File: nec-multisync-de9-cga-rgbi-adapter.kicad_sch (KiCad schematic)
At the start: 2 parts, among them J1 DE9_Plug, J2 DE15_Receptacle_HighDensity

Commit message: V1 to Fab
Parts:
- added J3: DIN-8, CUI_SDS_80J:CUI_SDS-80J, symbol Connector:DIN-8
- added JP1, JP4, JP5, JP6, JP7: Jumper_2_Bridged, Jumper:SolderJumper-2_P1.3mm_Bridged_Pad1.0x1.5mm, symbol Jumper:Jumper_2_Bridged
- J1: footprint (none) -> Connector_Dsub:DSUB-9_Male_Horizontal_P2.77x2.84mm_EdgePinOffset7.70mm_Housed_MountingHolesOffset9.12mm
- J2: footprint (none) -> Connector_TE_AMP_HD15:FIXED-1-1734530-1
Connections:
- net EGA_Blue0: now also J3.8
- net EGA_Green0: now also JP6.1 (A)
- net EGA_Green1_Intensity: now also JP1.2 (B)
- net EGA_Red0: now also JP7.2 (B)
- net GND: now also J3.2
- net HSync: now also JP5.1 (A)
- net VSync: now also JP4.2 (B)
- new net: J3.5, JP5.2 (B)
- new net: J3.6, JP6.2 (B)
- new net: J3.7, JP7.1 (A)
- new net: J3.1, JP1.1 (A)
- new net: J3.4, JP4.1 (A)
- no-connect marks 6 -> 7
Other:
- note added: "From IBM PC"
- note added: "From Japanese PC"
- note added: "NOT ACCURATE PIN NUMBERS Flipped from reality because we expect a male-male cable"
- note removed: "TODO: Din8"
- note removed: "To IBM PC"

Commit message: Update to NOTWORKING
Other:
- note added: "TODO: This does not work on MultiSync 3D yet (no wakeup)"
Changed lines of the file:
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@@
+    (effects (font (size 1.27 1.27)) (justify left bottom))
+  )
+  (text "TODO: This does not work on MultiSync 3D yet (no wakeup)"
+    (at 92.71 131.445 0)
     (effects (font (size 1.27 1.27)) (justify left bottom))
   )

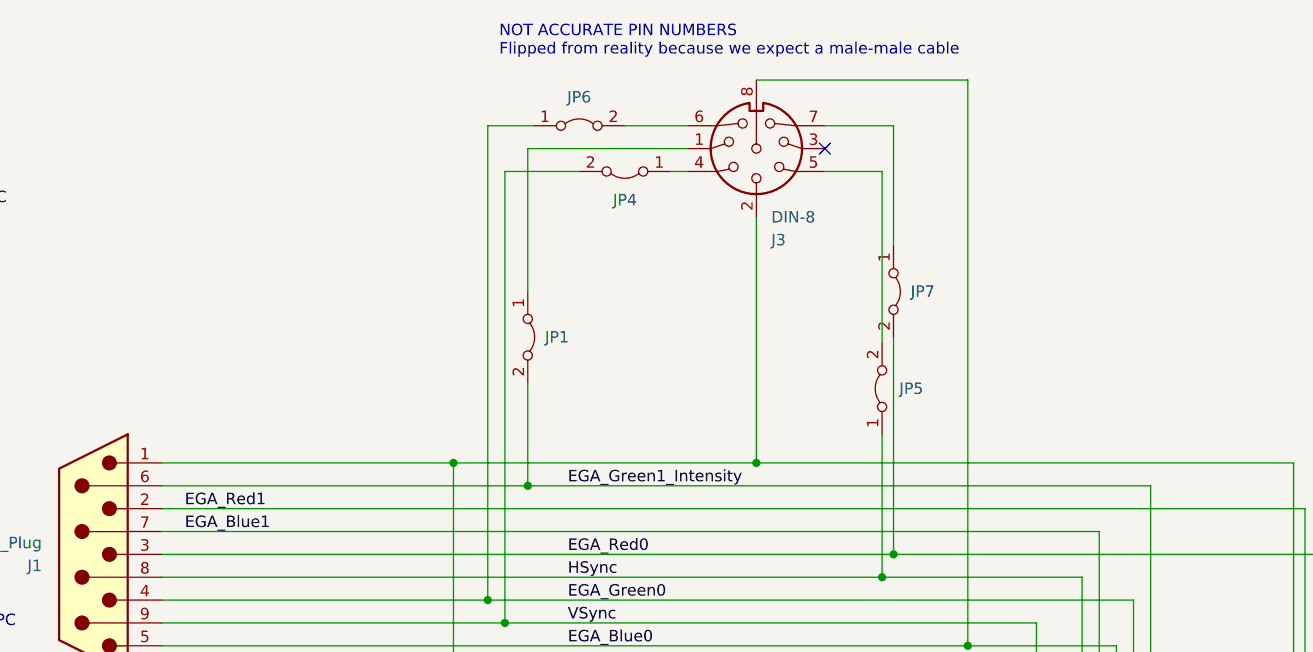
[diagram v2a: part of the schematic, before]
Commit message: Maybe reverse my bonehead fuckup of feeding 12V to the MultiSync's signal input
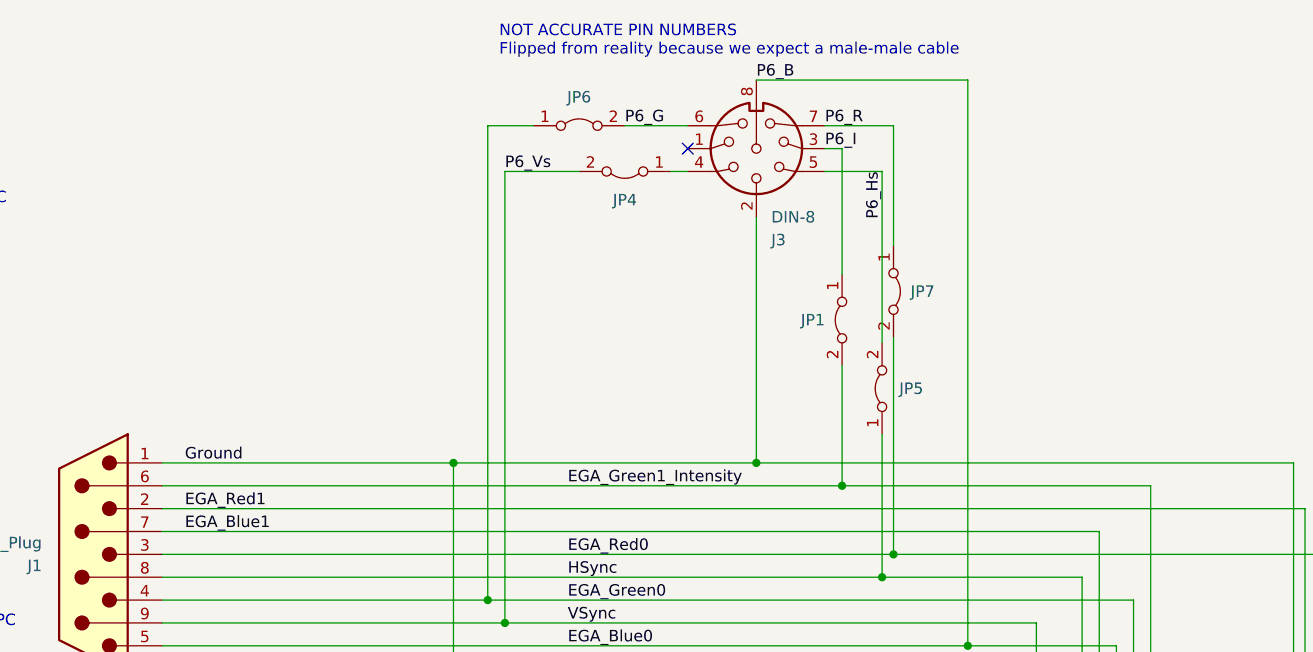
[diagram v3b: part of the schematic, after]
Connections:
- net P6_Hs: now reaches J3.5, JP5.2 (B)
- net P6_G: now reaches J3.6, JP6.2 (B)
- net P6_R: now reaches J3.7, JP7.1 (A)
- net at J3.1: no longer JP1.1 (A)
- net P6_I: now reaches J3.3
- net P6_I: now also JP1.1 (A)
- net VSync renamed P6_Vs
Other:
- moved on the sheet: JP1
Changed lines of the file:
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@@
   (junction (at 88.9 67.31) (diameter 0) (color 0 0 0 0)
   )
+  (junction (at 132.08 69.85) (diameter 0) (color 0 0 0 0)
+  )
   (junction (at 122.555 67.31) (diameter 0) (color 0 0 0 0)
-  )
-  (junction (at 97.155 69.85) (diameter 0) (color 0 0 0 0)
   )
   (junction (at 137.795 77.47) (diameter 0) (color 0 0 0 0)
@@
   (no_connect (at 195.58 102.235))
   (no_connect (at 195.58 97.155))
-  (no_connect (at 130.175 32.385))
   (no_connect (at 195.58 104.775))
   (no_connect (at 210.82 89.535))
   (no_connect (at 195.58 92.075))
+  (no_connect (at 114.935 32.385))
   (wire (pts (xy 137.795 29.845) (xy 137.795 43.18))
     (stroke (width 0) (type default))
   )
-  (wire (pts (xy 114.935 32.385) (xy 97.155 32.385))
+  (wire (pts (xy 132.08 69.85) (xy 166.37 69.85))
     (stroke (width 0) (type default))
   )
@@
     (stroke (width 0) (type default))
   )
-  (wire (pts (xy 97.155 32.385) (xy 97.155 48.26))
-    (stroke (width 0) (type default))
-  )
   (wire (pts (xy 226.695 104.775) (xy 210.82 104.775))
     (stroke (width 0) (type default))
   )
+  (wire (pts (xy 132.08 56.515) (xy 132.08 69.85))
+    (stroke (width 0) (type default))
+  )
   (wire (pts (xy 122.555 40.005) (xy 122.555 67.31))
     (stroke (width 0) (type default))
@@
     (stroke (width 0) (type default))
   )
-  (wire (pts (xy 97.155 58.42) (xy 97.155 69.85))
-    (stroke (width 0) (type default))
-  )
   (wire (pts (xy 164.465 82.55) (xy 164.465 132.715))
     (stroke (width 0) (type default))
@@
     (stroke (width 0) (type default))
   )
+  (wire (pts (xy 132.08 32.385) (xy 132.08 46.355))
+    (stroke (width 0) (type default))
+  )
   (wire (pts (xy 166.37 69.85) (xy 166.37 109.855))
     (stroke (width 0) (type default))
@@
     (stroke (width 0) (type default))
   )
-  (wire (pts (xy 97.155 69.85) (xy 166.37 69.85))
-    (stroke (width 0) (type default))
-  )
   (wire (pts (xy 130.175 29.845) (xy 137.795 29.845))
     (stroke (width 0) (type default))
@@
     (stroke (width 0) (type default))
   )
+  (wire (pts (xy 130.175 32.385) (xy 132.08 32.385))
+    (stroke (width 0) (type default))
+  )
   (wire (pts (xy 56.515 80.01) (xy 136.525 80.01))
     (stroke (width 0) (type default))
@@
     (stroke (width 0) (type default))
   )
-  (wire (pts (xy 56.515 69.85) (xy 97.155 69.85))
+  (wire (pts (xy 56.515 69.85) (xy 132.08 69.85))
     (stroke (width 0) (type default))
   )
@@
     (effects (font (size 1.27 1.27)) (justify left bottom))
   )
+  (label "P6_G" (at 107.95 29.845 0) (fields_autoplaced)
+    (effects (font (size 1.27 1.27)) (justify left bottom))
+  )
   (label "EGA_Blue1" (at 59.055 74.93 0) (fields_autoplaced)
     (effects (font (size 1.27 1.27)) (justify left bottom))
@@
     (effects (font (size 1.27 1.27)) (justify left bottom))
   )
+  (label "P6_I" (at 130.175 32.385 0) (fields_autoplaced)
+    (effects (font (size 1.27 1.27)) (justify left bottom))
+  )
+  (label "P6_Hs" (at 136.525 34.925 270) (fields_autoplaced)
+    (effects (font (size 1.27 1.27)) (justify right bottom))
+  )
+  (label "P6_B" (at 122.555 24.765 0) (fields_autoplaced)
+    (effects (font (size 1.27 1.27)) (justify left bottom))
+  )
+  (label "P6_R" (at 130.175 29.845 0) (fields_autoplaced)
+    (effects (font (size 1.27 1.27)) (justify left bottom))
+  )
   (label "EGA_Red0" (at 101.6 77.47 0) (fields_autoplaced)
     (effects (font (size 1.27 1.27)) (justify left bottom))
   )
+  (label "Ground" (at 59.055 67.31 0) (fields_autoplaced)
+    (effects (font (size 1.27 1.27)) (justify left bottom))
+  )
   (label "EGA_Red1" (at 59.055 72.39 0) (fields_autoplaced)
     (effects (font (size 1.27 1.27)) (justify left bottom))
@@
   )
   (label "HSync" (at 101.6 80.01 0) (fields_autoplaced)
+    (effects (font (size 1.27 1.27)) (justify left bottom))
+  )
+  (label "P6_Vs" (at 94.615 34.925 0) (fields_autoplaced)
     (effects (font (size 1.27 1.27)) (justify left bottom))
   )
@@
     )
   )
-  (symbol (lib_id "Jumper:Jumper_2_Bridged") (at 97.155 53.34 270) (unit 1)
-    (in_bom yes) (on_board yes) (dnp no) (fields_autoplaced)
-    (property "Reference" "JP1" (at 99.06 53.34 90)
+  (symbol (lib_id "Jumper:Jumper_2_Bridged") (at 132.08 51.435 90) (mirror x) (unit 1)
+    (in_bom yes) (on_board yes) (dnp no)
+    (property "Reference" "JP1" (at 130.175 51.435 90)
       (effects (font (size 1.27 1.27)) (justify left))
     )
-    (property "Value" "Jumper_2_Bridged" (at 99.06 54.61 90)
+    (property "Value" "Jumper_2_Bridged" (at 130.175 52.705 90)
       (effects (font (size 1.27 1.27)) (justify left) hide)
     )
-    (property "Footprint" "Jumper:SolderJumper-2_P1.3mm_Bridged_Pad1.0x1.5mm" (at 97.155 53.34 0)
-      (effects (font (size 1.27 1.27)) hide)
-    )
-    (property "Datasheet" "~" (at 97.155 53.34 0)
-      (effects (font (size 1.27 1.27)) hide)
-    )
+    (property "Footprint" "Jumper:SolderJumper-2_P1.3mm_Bridged_Pad1.0x1.5mm" (at 132.08 51.435 0)
+      (effects (font (size 1.27 1.27)) hide)
+    )
+    (property "Datasheet" "~" (at 132.08 51.435 0)
+      (effects (font (size 1.27 1.27)) hide)
+    )

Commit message: Label nets
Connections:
- net P6_I: now also J3.1; no longer J3.3
- net P6_Vs: now also J3.4, JP4.1 (A); no longer J1.9, J2.10, JP4.2 (B)
- new net VSync: J1.9, J2.10, JP4.2 (B)
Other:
- moved on the sheet: JP1, JP4
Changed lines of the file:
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@@
   (junction (at 88.9 67.31) (diameter 0) (color 0 0 0 0)
   )
-  (junction (at 132.08 69.85) (diameter 0) (color 0 0 0 0)
-  )
   (junction (at 122.555 67.31) (diameter 0) (color 0 0 0 0)
+  )
+  (junction (at 99.695 69.85) (diameter 0) (color 0 0 0 0)
   )
   (junction (at 137.795 77.47) (diameter 0) (color 0 0 0 0)
@@
   (no_connect (at 195.58 102.235))
   (no_connect (at 195.58 97.155))
+  (no_connect (at 130.175 32.385))
   (no_connect (at 195.58 104.775))
   (no_connect (at 210.82 89.535))
   (no_connect (at 195.58 92.075))
-  (no_connect (at 114.935 32.385))
   (wire (pts (xy 137.795 29.845) (xy 137.795 43.18))
     (stroke (width 0) (type default))
   )
-  (wire (pts (xy 132.08 69.85) (xy 166.37 69.85))
+  (wire (pts (xy 56.515 69.85) (xy 99.695 69.85))
     (stroke (width 0) (type default))
   )
@@
     (stroke (width 0) (type default))
   )
+  (wire (pts (xy 99.695 69.85) (xy 166.37 69.85))
+    (stroke (width 0) (type default))
+  )
   (wire (pts (xy 226.695 104.775) (xy 210.82 104.775))
     (stroke (width 0) (type default))
   )
-  (wire (pts (xy 132.08 56.515) (xy 132.08 69.85))
-    (stroke (width 0) (type default))
-  )
   (wire (pts (xy 122.555 40.005) (xy 122.555 67.31))
     (stroke (width 0) (type default))
@@
     (stroke (width 0) (type default))
   )
-  (wire (pts (xy 102.87 34.925) (xy 94.615 34.925))
-    (stroke (width 0) (type default))
-  )
   (wire (pts (xy 182.245 67.31) (xy 182.245 89.535))
     (stroke (width 0) (type default))
@@
     (stroke (width 0) (type default))
   )
-  (wire (pts (xy 132.08 32.385) (xy 132.08 46.355))
-    (stroke (width 0) (type default))
-  )
   (wire (pts (xy 166.37 69.85) (xy 166.37 109.855))
     (stroke (width 0) (type default))
@@
     (stroke (width 0) (type default))
   )
+  (wire (pts (xy 106.045 32.385) (xy 114.935 32.385))
+    (stroke (width 0) (type default))
+  )
+  (wire (pts (xy 106.045 46.99) (xy 106.045 32.385))
+    (stroke (width 0) (type default))
+  )
   (wire (pts (xy 130.175 29.845) (xy 137.795 29.845))
     (stroke (width 0) (type default))
@@
     (stroke (width 0) (type default))
   )
+  (wire (pts (xy 106.045 57.15) (xy 99.695 57.15))
+    (stroke (width 0) (type default))
+  )
   (wire (pts (xy 224.79 132.715) (xy 224.79 99.695))
     (stroke (width 0) (type default))
@@
     (stroke (width 0) (type default))
   )
-  (wire (pts (xy 130.175 32.385) (xy 132.08 32.385))
-    (stroke (width 0) (type default))
-  )
   (wire (pts (xy 56.515 80.01) (xy 136.525 80.01))
     (stroke (width 0) (type default))
@@
     (stroke (width 0) (type default))
   )
+  (wire (pts (xy 99.695 57.15) (xy 99.695 69.85))
+    (stroke (width 0) (type default))
+  )
   (wire (pts (xy 210.82 99.695) (xy 224.79 99.695))
     (stroke (width 0) (type default))
@@
     (stroke (width 0) (type default))
   )
-  (wire (pts (xy 114.935 34.925) (xy 113.03 34.925))
+  (wire (pts (xy 114.935 34.925) (xy 104.775 34.925))
     (stroke (width 0) (type default))
   )
@@
   )
   (wire (pts (xy 153.67 107.315) (xy 195.58 107.315))
-    (stroke (width 0) (type default))
-  )
-  (wire (pts (xy 56.515 69.85) (xy 132.08 69.85))
     (stroke (width 0) (type default))
   )
@@
     (effects (font (size 1.27 1.27)) (justify left bottom))
   )
-  (label "P6_I" (at 130.175 32.385 0) (fields_autoplaced)
+  (label "P6_I" (at 106.045 44.45 90) (fields_autoplaced)
     (effects (font (size 1.27 1.27)) (justify left bottom))
   )
@@
     (effects (font (size 1.27 1.27)) (justify left bottom))
   )
-  (label "P6_Vs" (at 94.615 34.925 0) (fields_autoplaced)
+  (label "P6_Vs" (at 107.95 34.925 0) (fields_autoplaced)
     (effects (font (size 1.27 1.27)) (justify left bottom))
   )
@@
     )
   )
-  (symbol (lib_id "Jumper:Jumper_2_Bridged") (at 132.08 51.435 90) (mirror x) (unit 1)
+  (symbol (lib_id "Jumper:Jumper_2_Bridged") (at 106.045 52.07 90) (mirror x) (unit 1)
     (in_bom yes) (on_board yes) (dnp no)
-    (property "Reference" "JP1" (at 130.175 51.435 90)
+    (property "Reference" "JP1" (at 104.14 52.07 90)
       (effects (font (size 1.27 1.27)) (justify left))
     )
-    (property "Value" "Jumper_2_Bridged" (at 130.175 52.705 90)
+    (property "Value" "Jumper_2_Bridged" (at 104.14 53.34 90)
       (effects (font (size 1.27 1.27)) (justify left) hide)
     )
-    (property "Footprint" "Jumper:SolderJumper-2_P1.3mm_Bridged_Pad1.0x1.5mm" (at 132.08 51.435 0)
-      (effects (font (size 1.27 1.27)) hide)
-    )
-    (property "Datasheet" "~" (at 132.08 51.435 0)
+    (property "Footprint" "Jumper:SolderJumper-2_P1.3mm_Bridged_Pad1.0x1.5mm" (at 106.045 52.07 0)
+      (effects (font (size 1.27 1.27)) hide)
+    )
+    (property "Datasheet" "~" (at 106.045 52.07 0)
       (effects (font (size 1.27 1.27)) hide)
     )
@@
     )
   )
-  (symbol (lib_id "Jumper:Jumper_2_Bridged") (at 107.95 34.925 180) (unit 1)
+  (symbol (lib_id "Jumper:Jumper_2_Bridged") (at 99.695 34.925 180) (unit 1)
     (in_bom yes) (on_board yes) (dnp no)
-    (property "Reference" "JP4" (at 107.95 38.1 0)
+    (property "Reference" "JP4" (at 99.695 38.1 0)
       (effects (font (size 1.27 1.27)))
     )
-    (property "Value" "Jumper_2_Bridged" (at 107.95 31.75 0)
-      (effects (font (size 1.27 1.27)) hide)
-    )
-    (property "Footprint" "Jumper:SolderJumper-2_P1.3mm_Bridged_Pad1.0x1.5mm" (at 107.95 34.925 0)
-      (effects (font (size 1.27 1.27)) hide)
-    )
-    (property "Datasheet" "~" (at 107.95 34.925 0)
-      (effects (font (size 1.27 1.27)) hide)
-    )
+    (property "Value" "Jumper_2_Bridged" (at 99.695 31.75 0)
+      (effects (font (size 1.27 1.27)) hide)
+    )
+    (property "Footprint" "Jumper:SolderJumper-2_P1.3mm_Bridged_Pad1.0x1.5mm" (at 99.695 34.925 0)
+      (effects (font (size 1.27 1.27)) hide)
+    )
+    (property "Datasheet" "~" (at 99.695 34.925 0)
+      (effects (font (size 1.27 1.27)) hide)
+    )
